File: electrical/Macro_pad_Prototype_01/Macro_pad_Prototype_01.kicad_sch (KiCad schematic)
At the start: 26 parts, among them SW1 SW_Push_45deg, SW10 SW_Push_45deg, SW11 SW_Push_45deg, SW12 SW_Push_45deg, SW13 SW_Push_45deg, SW2 SW_Push_45deg, SW3 SW_Push_45deg, SW4 SW_Push_45deg, SW5 SW_Push_45deg, SW6 SW_Push_45deg, SW7 SW_Push_45deg, SW8 SW_Push_45deg, SW9 SW_Push_45deg

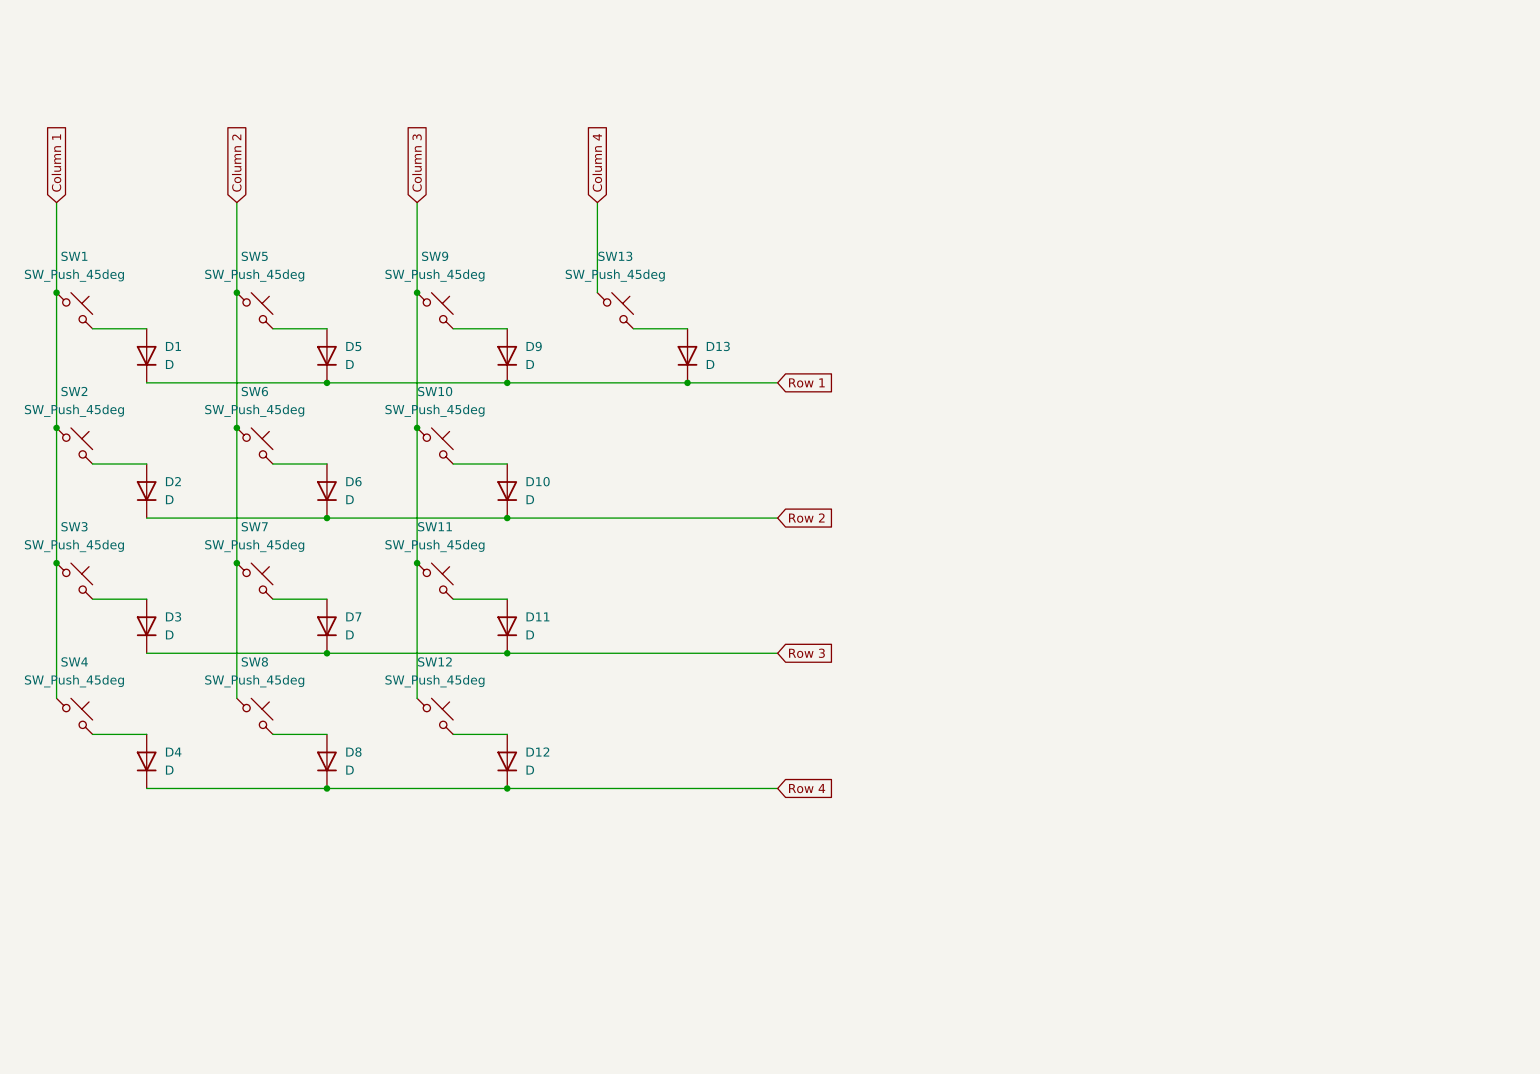
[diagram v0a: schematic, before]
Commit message: base layout complete
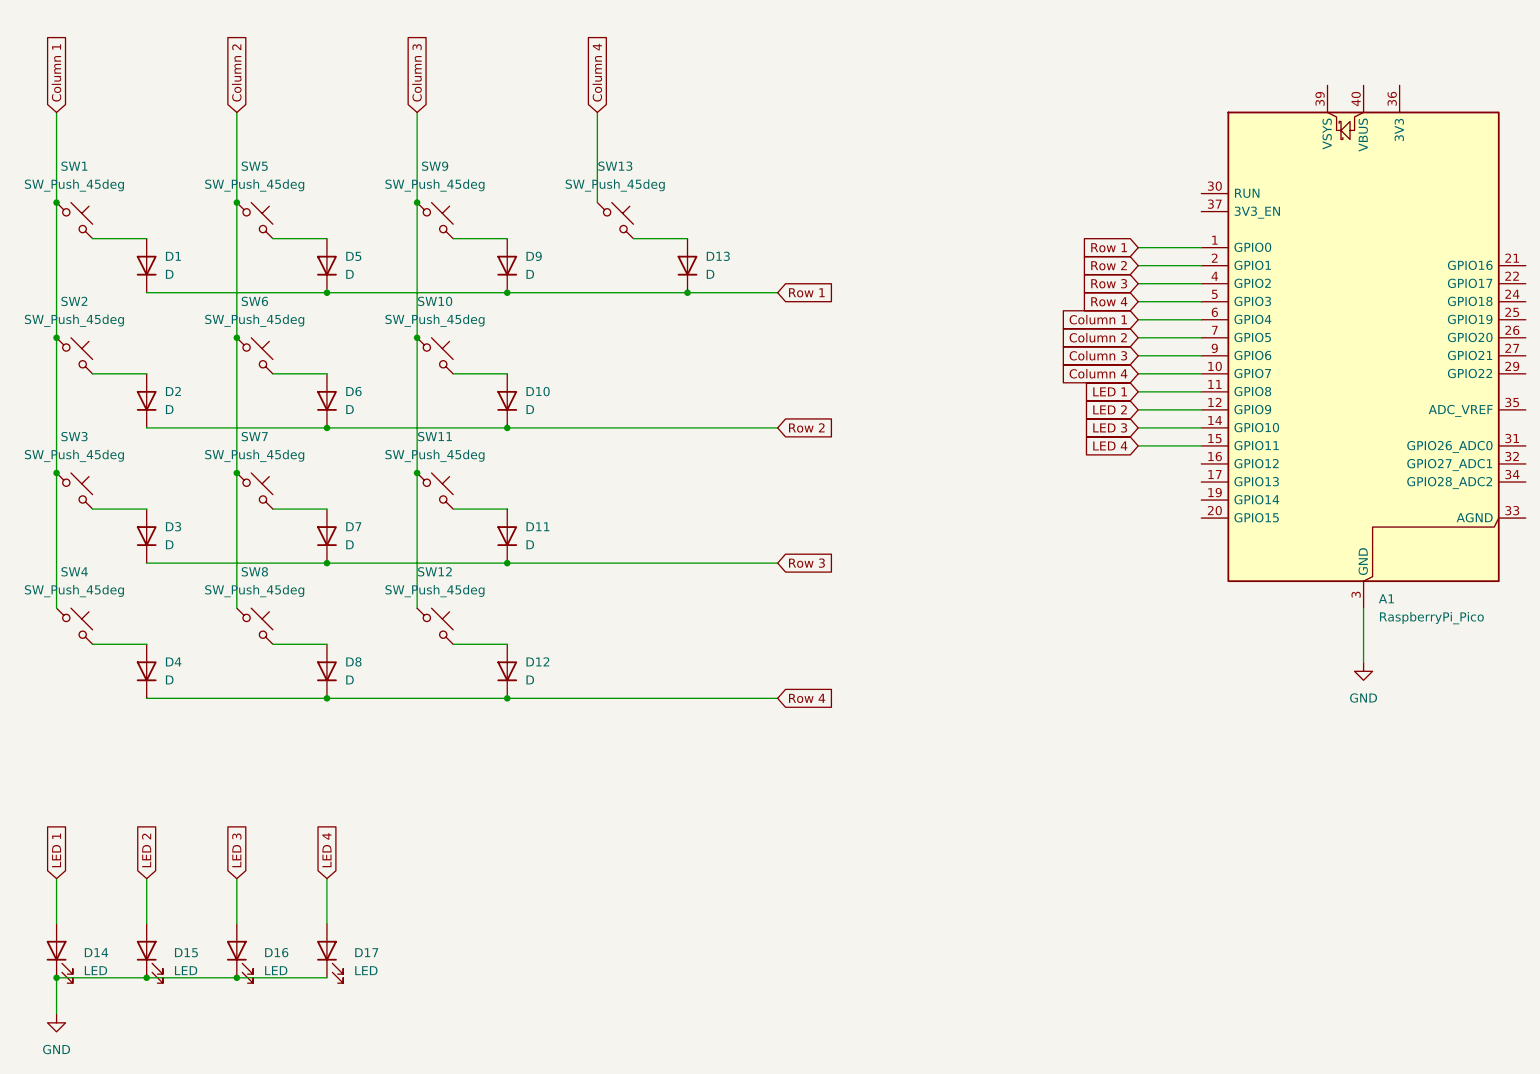
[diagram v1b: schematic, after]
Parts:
- added A1: RaspberryPi_Pico, Module:RaspberryPi_Pico_Common_Unspecified, symbol MCU_Module:RaspberryPi_Pico
- added D14, D15, D16, D17: LED, LED_SMD:LED_1206_3216Metric_Pad1.42x1.75mm_HandSolder, symbol Device:LED
- D1, D10, D11, D12, D13, D2, D3, D4, D5, D6, D7, D8, D9: footprint (none) -> Diode_SMD:D_SOD-123
- SW1, SW10, SW11, SW12, SW13, SW2, SW3, SW4, SW5, SW6, SW7, SW8, SW9: footprint (none) -> PCM_Switch_Keyboard_Cherry_MX:SW_Cherry_MX_PCB_1.00u
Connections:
- net Column 1: now also A1.6 (GPIO4)
- net Column 2: now also A1.7 (GPIO5)
- net Column 3: now also A1.9 (GPIO6)
- net Column 4: now also A1.10 (GPIO7)
- net Row 1: now also A1.1 (GPIO0)
- net Row 2: now also A1.2 (GPIO1)
- net Row 3: now also A1.4 (GPIO2)
- net Row 4: now also A1.5 (GPIO3)
- new net GND: A1.13 (GND), A1.18 (GND), A1.23 (GND), A1.28 (GND), A1.3 (GND), A1.38 (GND), A1.8 (GND), D14.1 (K), D15.1 (K), D16.1 (K), D17.1 (K)
- new net LED 1: A1.11 (GPIO8), D14.2 (A)
- new net LED 2: A1.12 (GPIO9), D15.2 (A)
- new net LED 3: A1.14 (GPIO10), D16.2 (A)
- new net LED 4: A1.15 (GPIO11), D17.2 (A)
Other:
- moved on the sheet: D1, D10, D11, D12, D13, D2, D3, D4, D5, D6, D7, D8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
